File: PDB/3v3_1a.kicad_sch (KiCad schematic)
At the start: 13 parts, among them U17 INA228, U3 TLV62569ADRLR

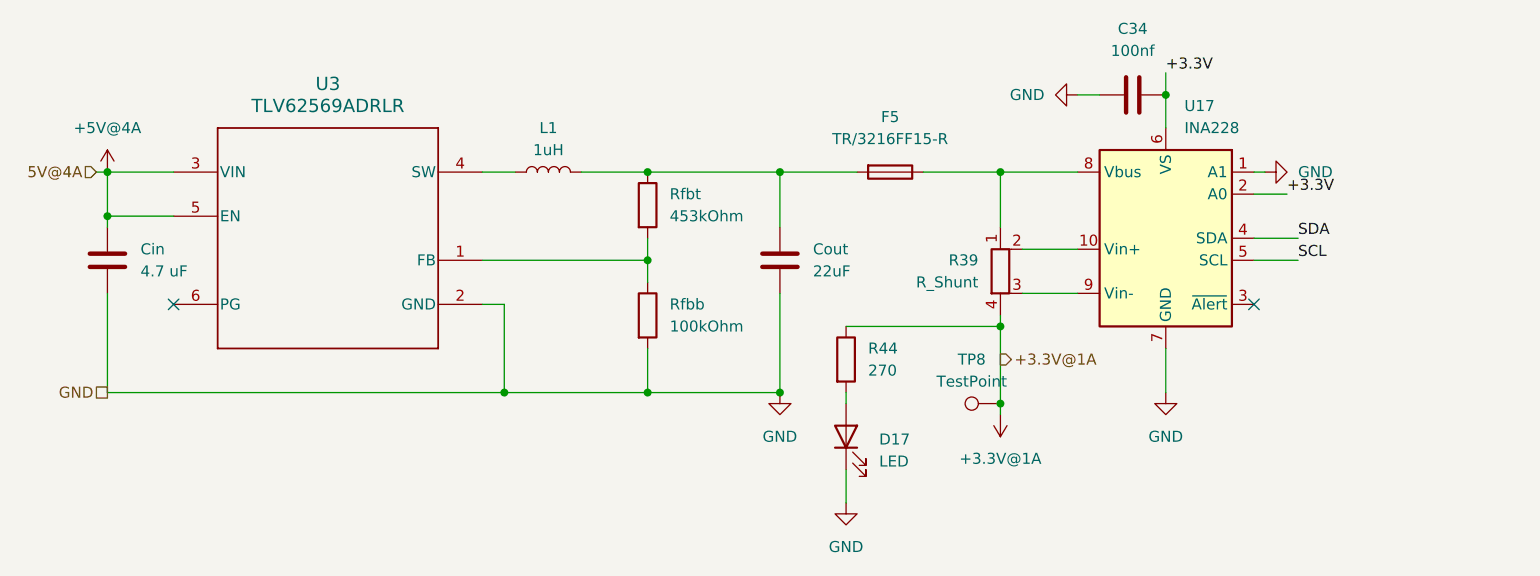
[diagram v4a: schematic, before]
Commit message: Finished all the footprints. doing poe myself now
finally.
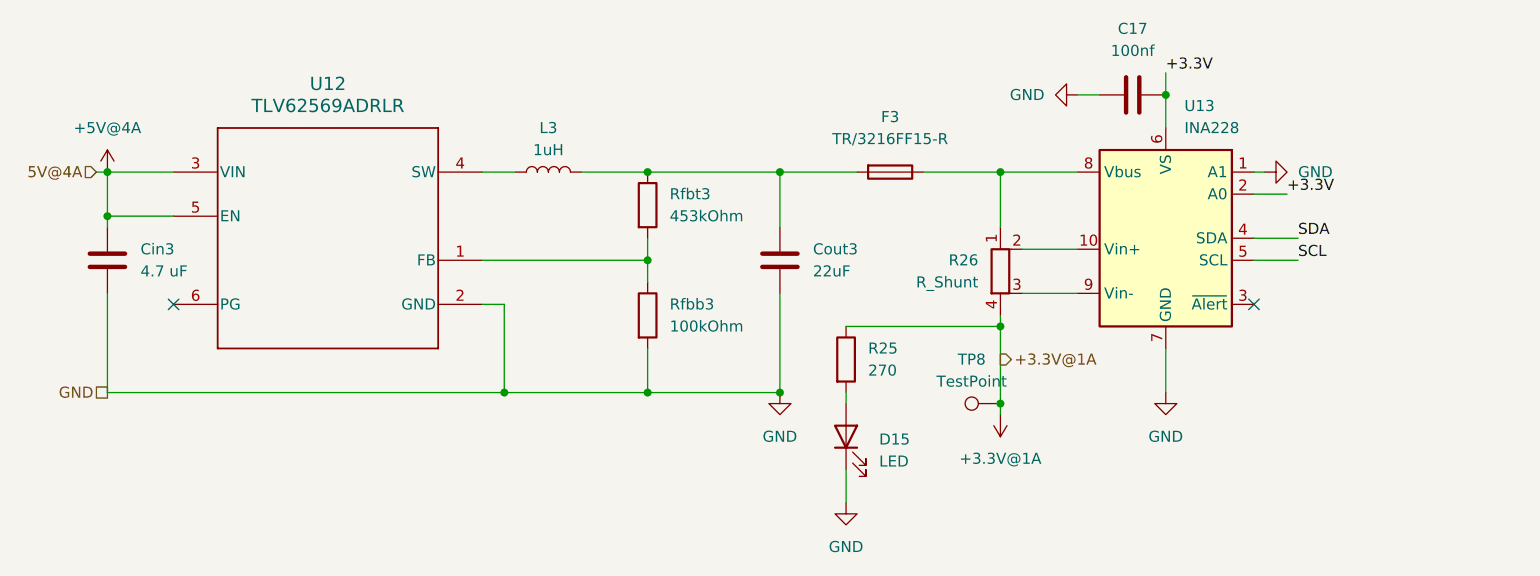
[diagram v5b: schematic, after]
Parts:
- C17: renamed from C34; footprint Capacitor_SMD:C_1206_3216Metric -> Capacitor_SMD:C_0603_1608Metric
- Cin3: renamed from Cin; footprint (none) -> Capacitor_SMD:C_0603_1608Metric
- Cout3: renamed from Cout; footprint (none) -> Capacitor_SMD:C_0603_1608Metric
- F3: renamed from F5; footprint (none) -> Fuse:Fuse_1206_3216Metric
- L3: renamed from L1; footprint (none) -> Inductor_SMD:L_1206_3216Metric
- R25: renamed from R44; footprint Resistor_SMD:R_1206_3216Metric_Pad1.30x1.75mm_HandSolder -> Resistor_SMD:R_0603_1608Metric
- R26: renamed from R39; footprint (none) -> Resistor_SMD:R_0603_1608Metric
- Rfbb3: renamed from Rfbb; footprint (none) -> Resistor_SMD:R_0603_1608Metric
- Rfbt3: renamed from Rfbt; footprint (none) -> Resistor_SMD:R_0603_1608Metric
- U12: renamed from U3; footprint DRL0006A -> Dependencies:TLV62569ADRLR
- U13: renamed from U17; footprint Package_SO:TSSOP-10_3x3mm_P0.5mm -> Package_SO:HVSSOP-10-1EP_3x3mm_P0.5mm_EP1.83x1.89mm
- renumbered D17 to D15
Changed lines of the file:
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@@
 		(dnp no)
 		(fields_autoplaced yes)
-		(property "Reference" "C34"
+		(property "Reference" "C17"
 			(at 151.13 43.18 90)
 			(show_name no)
@@
 			)
 		)
-		(property "Footprint" "Capacitor_SMD:C_1206_3216Metric"
+		(property "Footprint" "Capacitor_SMD:C_0603_1608Metric"
 			(at 154.94 49.8348 0)
 			(hide yes)
@@
 			(project "PDB"
 				(path "/a9cf05c4-aac5-4cf1-b700-1d3045f8dfbd/eaf0840f-875c-44d4-b065-16bc98c2c6be"
-					(reference "C34")
+					(reference "C17")
 					(unit 1)
 				)
@@
 		(dnp no)
 		(fields_autoplaced yes)
-		(property "Reference" "Cin"
+		(property "Reference" "Cin3"
 			(at 36.83 68.5799 0)
 			(show_name no)
@@
 			)
 		)
-		(property "Footprint" ""
+		(property "Footprint" "Capacitor_SMD:C_0603_1608Metric"
 			(at 33.9852 73.66 0)
 			(hide yes)
@@
 			(project "PDB"
 				(path "/a9cf05c4-aac5-4cf1-b700-1d3045f8dfbd/eaf0840f-875c-44d4-b065-16bc98c2c6be"
-					(reference "Cin")
+					(reference "Cin3")
 					(unit 1)
 				)
@@
 		(dnp no)
 		(fields_autoplaced yes)
-		(property "Reference" "U3"
+		(property "Reference" "U12"
 			(at 58.42 49.53 0)
 			(show_name no)
@@
 			)
 		)
-		(property "Footprint" "DRL0006A"
+		(property "Footprint" "Dependencies:TLV62569ADRLR"
 			(at 58.42 67.31 0)
 			(hide yes)
@@
 			(project "PDB"
 				(path "/a9cf05c4-aac5-4cf1-b700-1d3045f8dfbd/eaf0840f-875c-44d4-b065-16bc98c2c6be"
-					(reference "U3")
+					(reference "U12")
 					(unit 1)
 				)
@@
 		(dnp no)
 		(fields_autoplaced yes)
-		(property "Reference" "Rfbt"
+		(property "Reference" "Rfbt3"
 			(at 97.79 62.2299 0)
 			(show_name no)
@@
 			)
 		)
-		(property "Footprint" ""
+		(property "Footprint" "Resistor_SMD:R_0603_1608Metric"
 			(at 93.472 63.5 90)
 			(hide yes)
@@
 			(project "PDB"
 				(path "/a9cf05c4-aac5-4cf1-b700-1d3045f8dfbd/eaf0840f-875c-44d4-b065-16bc98c2c6be"
-					(reference "Rfbt")
+					(reference "Rfbt3")
 					(unit 1)
 				)
@@
 		(dnp no)
 		(fields_autoplaced yes)
-		(property "Reference" "R39"
+		(property "Reference" "R26"
 			(at 133.35 69.8499 0)
 			(show_name no)
@@
 			)
 		)
-		(property "Footprint" ""
+		(property "Footprint" "Resistor_SMD:R_0603_1608Metric"
 			(at 134.112 71.12 90)
 			(hide yes)
@@
 			(project "PDB"
 				(path "/a9cf05c4-aac5-4cf1-b700-1d3045f8dfbd/eaf0840f-875c-44d4-b065-16bc98c2c6be"
-					(reference "R39")
+					(reference "R26")
 					(unit 1)
 				)
@@
 		(dnp no)
 		(fields_autoplaced yes)
-		(property "Reference" "F5"
+		(property "Reference" "F3"
 			(at 123.19 53.34 90)
 			(show_name no)
@@
 			)
 		)
-		(property "Footprint" ""
+		(property "Footprint" "Fuse:Fuse_1206_3216Metric"
 			(at 123.19 57.912 90)
 			(hide yes)
@@
 			(project "PDB"
 				(path "/a9cf05c4-aac5-4cf1-b700-1d3045f8dfbd/eaf0840f-875c-44d4-b065-16bc98c2c6be"
-					(reference "F5")
+					(reference "F3")
 					(unit 1)
 				)
@@
 		(dnp no)
 		(fields_autoplaced yes)
-		(property "Reference" "Cout"
+		(property "Reference" "Cout3"
 			(at 114.3 68.5799 0)
 			(show_name no)
@@
 			)
 		)
-		(property "Footprint" ""
+		(property "Footprint" "Capacitor_SMD:C_0603_1608Metric"
 			(at 111.4552 73.66 0)
 			(hide yes)
@@
 			(project "PDB"
 				(path "/a9cf05c4-aac5-4cf1-b700-1d3045f8dfbd/eaf0840f-875c-44d4-b065-16bc98c2c6be"
-					(reference "Cout")
+					(reference "Cout3")
 					(unit 1)
 				)
@@
 		(in_pos_files yes)
 		(dnp no)
-		(property "Reference" "R44"
+		(property "Reference" "R25"
 			(at 120.65 80.0099 0)
 			(show_name no)
@@
 			)
 		)
-		(property "Footprint" "Resistor_SMD:R_1206_3216Metric_Pad1.30x1.75mm_HandSolder"
+		(property "Footprint" "Resistor_SMD:R_0603_1608Metric"
 			(at 116.332 81.28 90)
 			(hide yes)
@@
 			(project "PDB"
 				(path "/a9cf05c4-aac5-4cf1-b700-1d3045f8dfbd/eaf0840f-875c-44d4-b065-16bc98c2c6be"
-					(reference "R44")
+					(reference "R25")
 					(unit 1)
 				)
@@
 		(dnp no)
 		(fields_autoplaced yes)
-		(property "Reference" "Rfbb"
+		(property "Reference" "Rfbb3"
 			(at 97.79 74.9299 0)
 			(show_name no)
@@
 			)
 		)
-		(property "Footprint" ""
+		(property "Footprint" "Resistor_SMD:R_0603_1608Metric"
 			(at 93.472 76.2 90)
 			(hide yes)
@@
 			(project "PDB"
 				(path "/a9cf05c4-aac5-4cf1-b700-1d3045f8dfbd/eaf0840f-875c-44d4-b065-16bc98c2c6be"
-					(reference "Rfbb")
+					(reference "Rfbb3")
 					(unit 1)
 				)
@@
 		(dnp no)
 		(fields_autoplaced yes)
-		(property "Reference" "L1"
+		(property "Reference" "L3"
 			(at 83.82 54.61 90)
 			(show_name no)
@@
 			)
 		)
-		(property "Footprint" ""
+		(property "Footprint" "Inductor_SMD:L_1206_3216Metric"
 			(at 83.82 59.69 0)
 			(hide yes)
@@
 			(project "PDB"
 				(path "/a9cf05c4-aac5-4cf1-b700-1d3045f8dfbd/eaf0840f-875c-44d4-b065-16bc98c2c6be"
-					(reference "L1")
+					(reference "L3")
 					(unit 1)
 				)
@@
 		(dnp no)
 		(fields_autoplaced yes)
-		(property "Reference" "D17"
+		(property "Reference" "D15"
 			(at 121.92 90.4874 90)
 			(show_name no)
@@
 			(project "PDB"
 				(path "/a9cf05c4-aac5-4cf1-b700-1d3045f8dfbd/eaf0840f-875c-44d4-b065-16bc98c2c6be"
-					(reference "D17")
+					(reference "D15")
 					(unit 1)
 				)
@@
 		(dnp no)
 		(fields_autoplaced yes)
-		(property "Reference" "U17"
+		(property "Reference" "U13"
 			(at 157.0833 52.07 0)
 			(show_name no)
@@
 			)
 		)
-		(property "Footprint" "Package_SO:TSSOP-10_3x3mm_P0.5mm"
+		(property "Footprint" "Package_SO:HVSSOP-10-1EP_3x3mm_P0.5mm_EP1.83x1.89mm"
 			(at 179.832 44.704 0)
 			(hide yes)
@@
 			(project "PDB"
 				(path "/a9cf05c4-aac5-4cf1-b700-1d3045f8dfbd/eaf0840f-875c-44d4-b065-16bc98c2c6be"
-					(reference "U17")
-					(unit 1)
-				)
+					(reference "U13")
+					(unit 1)
+				)

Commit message: fixed component footprints
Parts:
- R26: footprint Resistor_SMD:R_0603_1608Metric -> Resistor_SMD:R_Shunt_Vishay_WSR2_WSR3_KelvinConnection
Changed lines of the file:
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@@
 		(dnp no)
 		(fields_autoplaced yes)
-		(property "Reference" "#PWR06"
+		(property "Reference" "#PWR058"
 			(at 110.49 91.44 0)
 			(hide yes)
@@
 			(project "PDB"
 				(path "/a9cf05c4-aac5-4cf1-b700-1d3045f8dfbd/eaf0840f-875c-44d4-b065-16bc98c2c6be"
-					(reference "#PWR06")
+					(reference "#PWR058")
 					(unit 1)
 				)
@@
 		(dnp no)
 		(fields_autoplaced yes)
-		(property "Reference" "#PWR059"
+		(property "Reference" "#PWR063"
 			(at 172.72 59.69 0)
 			(hide yes)
@@
 			(project "PDB"
 				(path "/a9cf05c4-aac5-4cf1-b700-1d3045f8dfbd/eaf0840f-875c-44d4-b065-16bc98c2c6be"
-					(reference "#PWR059")
+					(reference "#PWR063")
 					(unit 1)
 				)
@@
 		(dnp no)
 		(fields_autoplaced yes)
-		(property "Reference" "#PWR060"
+		(property "Reference" "#PWR062"
 			(at 154.94 91.44 0)
 			(hide yes)
@@
 			(project "PDB"
 				(path "/a9cf05c4-aac5-4cf1-b700-1d3045f8dfbd/eaf0840f-875c-44d4-b065-16bc98c2c6be"
-					(reference "#PWR060")
+					(reference "#PWR062")
 					(unit 1)
 				)
@@
 			)
 		)
-		(property "Footprint" "Resistor_SMD:R_0603_1608Metric"
+		(property "Footprint" "Resistor_SMD:R_Shunt_Vishay_WSR2_WSR3_KelvinConnection"
 			(at 134.112 71.12 90)
 			(hide yes)
@@
 		(dnp no)
 		(fields_autoplaced yes)
-		(property "Reference" "#PWR09"
+		(property "Reference" "#PWR060"
 			(at 135.89 83.82 0)
 			(hide yes)
@@
 			(project "PDB"
 				(path "/a9cf05c4-aac5-4cf1-b700-1d3045f8dfbd/eaf0840f-875c-44d4-b065-16bc98c2c6be"
-					(reference "#PWR09")
+					(reference "#PWR060")
 					(unit 1)
 				)
@@
 		(dnp no)
 		(fields_autoplaced yes)
-		(property "Reference" "#PWR058"
+		(property "Reference" "#PWR061"
 			(at 138.43 50.8 0)
 			(hide yes)
@@
 			(project "PDB"
 				(path "/a9cf05c4-aac5-4cf1-b700-1d3045f8dfbd/eaf0840f-875c-44d4-b065-16bc98c2c6be"
-					(reference "#PWR058")
+					(reference "#PWR061")
 					(unit 1)
 				)
@@
 		(dnp no)
 		(fields_autoplaced yes)
-		(property "Reference" "#PWR05"
+		(property "Reference" "#PWR057"
 			(at 33.02 63.5 0)
 			(hide yes)
@@
 			(project "PDB"
 				(path "/a9cf05c4-aac5-4cf1-b700-1d3045f8dfbd/eaf0840f-875c-44d4-b065-16bc98c2c6be"
-					(reference "#PWR05")
+					(reference "#PWR057")
 					(unit 1)
 				)
@@
 		(dnp no)
 		(fields_autoplaced yes)
-		(property "Reference" "#PWR071"
+		(property "Reference" "#PWR059"
 			(at 118.11 104.14 0)
 			(hide yes)
@@
 			(project "PDB"
 				(path "/a9cf05c4-aac5-4cf1-b700-1d3045f8dfbd/eaf0840f-875c-44d4-b065-16bc98c2c6be"
-					(reference "#PWR071")
-					(unit 1)
-				)
+					(reference "#PWR059")
+					(unit 1)
+				)

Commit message: laid out many, many things
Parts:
- R26: footprint Resistor_SMD:R_Shunt_Vishay_WSR2_WSR3_KelvinConnection -> Resistor_SMD:R_Shunt_Vishay_WSK2512_6332Metric_T2.66mm
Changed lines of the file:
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@@
 			)
 		)
-		(property "Footprint" "Resistor_SMD:R_Shunt_Vishay_WSR2_WSR3_KelvinConnection"
+		(property "Footprint" "Resistor_SMD:R_Shunt_Vishay_WSK2512_6332Metric_T2.66mm"
 			(at 134.112 71.12 90)
 			(hide yes)

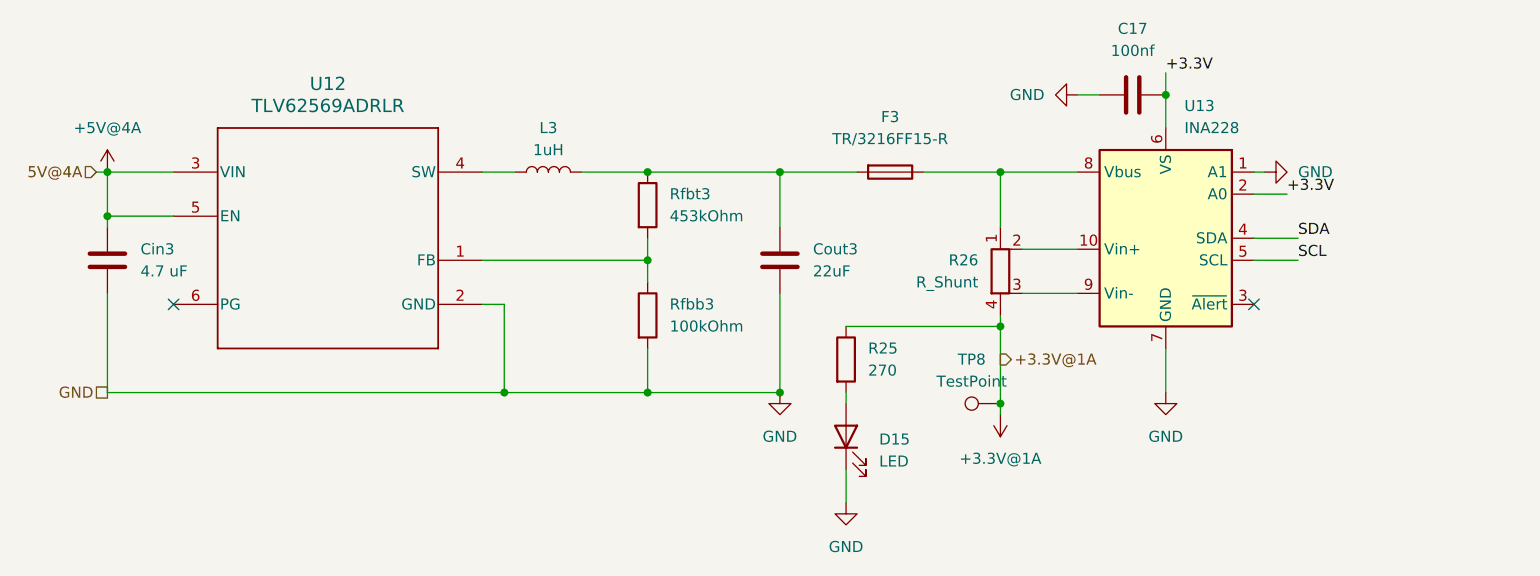
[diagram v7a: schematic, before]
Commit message: coordinated labels in schem
Labeled all components to be Rxx, Cxx, ext forms through all sheets so labels for BOM and layout are work together as one long list.
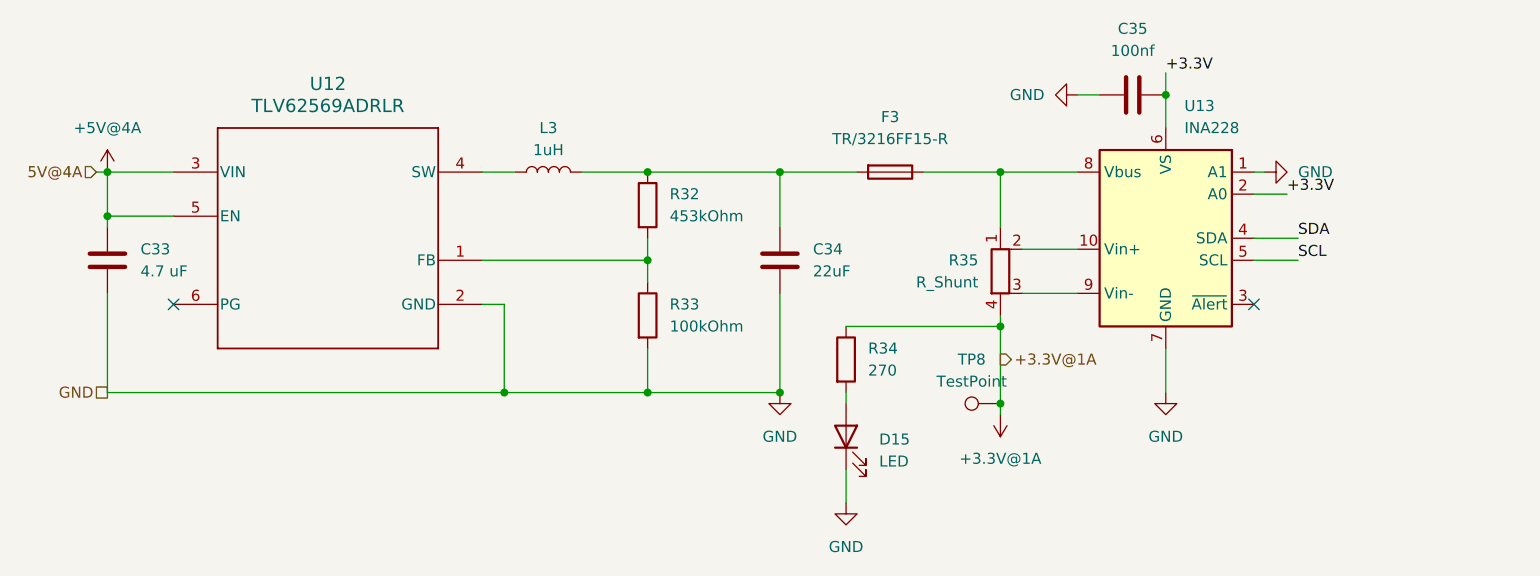
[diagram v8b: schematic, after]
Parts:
- renumbered Cin3 to C33, Cout3 to C34, C17 to C35, Rfbt3 to R32, Rfbb3 to R33, R25 to R34, R26 to R35
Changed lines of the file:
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@@
 		(dnp no)
 		(fields_autoplaced yes)
-		(property "Reference" "#PWR058"
+		(property "Reference" "#PWR059"
 			(at 110.49 91.44 0)
 			(hide yes)
@@
 			(project "PDB"
 				(path "/a9cf05c4-aac5-4cf1-b700-1d3045f8dfbd/eaf0840f-875c-44d4-b065-16bc98c2c6be"
-					(reference "#PWR058")
+					(reference "#PWR059")
 					(unit 1)
 				)
@@
 		(dnp no)
 		(fields_autoplaced yes)
-		(property "Reference" "C17"
+		(property "Reference" "C35"
 			(at 151.13 43.18 90)
 			(show_name no)
@@
 			(project "PDB"
 				(path "/a9cf05c4-aac5-4cf1-b700-1d3045f8dfbd/eaf0840f-875c-44d4-b065-16bc98c2c6be"
-					(reference "C17")
+					(reference "C35")
 					(unit 1)
 				)
@@
 		(dnp no)
 		(fields_autoplaced yes)
-		(property "Reference" "#PWR063"
+		(property "Reference" "#PWR064"
 			(at 172.72 59.69 0)
 			(hide yes)
@@
 			(project "PDB"
 				(path "/a9cf05c4-aac5-4cf1-b700-1d3045f8dfbd/eaf0840f-875c-44d4-b065-16bc98c2c6be"
-					(reference "#PWR063")
+					(reference "#PWR064")
 					(unit 1)
 				)
@@
 		(dnp no)
 		(fields_autoplaced yes)
-		(property "Reference" "Cin3"
+		(property "Reference" "C33"
 			(at 36.83 68.5799 0)
 			(show_name no)
@@
 			(project "PDB"
 				(path "/a9cf05c4-aac5-4cf1-b700-1d3045f8dfbd/eaf0840f-875c-44d4-b065-16bc98c2c6be"
-					(reference "Cin3")
+					(reference "C33")
 					(unit 1)
 				)
@@
 		(dnp no)
 		(fields_autoplaced yes)
-		(property "Reference" "#PWR062"
+		(property "Reference" "#PWR063"
 			(at 154.94 91.44 0)
 			(hide yes)
@@
 			(project "PDB"
 				(path "/a9cf05c4-aac5-4cf1-b700-1d3045f8dfbd/eaf0840f-875c-44d4-b065-16bc98c2c6be"
-					(reference "#PWR062")
+					(reference "#PWR063")
 					(unit 1)
 				)
@@
 		(dnp no)
 		(fields_autoplaced yes)
-		(property "Reference" "Rfbt3"
+		(property "Reference" "R32"
 			(at 97.79 62.2299 0)
 			(show_name no)
@@
 			(project "PDB"
 				(path "/a9cf05c4-aac5-4cf1-b700-1d3045f8dfbd/eaf0840f-875c-44d4-b065-16bc98c2c6be"
-					(reference "Rfbt3")
+					(reference "R32")
 					(unit 1)
 				)
@@
 		(dnp no)
 		(fields_autoplaced yes)
-		(property "Reference" "R26"
+		(property "Reference" "R35"
 			(at 133.35 69.8499 0)
 			(show_name no)
@@
 			(project "PDB"
 				(path "/a9cf05c4-aac5-4cf1-b700-1d3045f8dfbd/eaf0840f-875c-44d4-b065-16bc98c2c6be"
-					(reference "R26")
+					(reference "R35")
 					(unit 1)
 				)
@@
 		(dnp no)
 		(fields_autoplaced yes)
-		(property "Reference" "#PWR060"
+		(property "Reference" "#PWR061"
 			(at 135.89 83.82 0)
 			(hide yes)
@@
 			(project "PDB"
 				(path "/a9cf05c4-aac5-4cf1-b700-1d3045f8dfbd/eaf0840f-875c-44d4-b065-16bc98c2c6be"
-					(reference "#PWR060")
+					(reference "#PWR061")
 					(unit 1)
 				)
@@
 		(dnp no)
 		(fields_autoplaced yes)
-		(property "Reference" "#PWR061"
+		(property "Reference" "#PWR062"
 			(at 138.43 50.8 0)
 			(hide yes)
@@
 			(project "PDB"
 				(path "/a9cf05c4-aac5-4cf1-b700-1d3045f8dfbd/eaf0840f-875c-44d4-b065-16bc98c2c6be"
-					(reference "#PWR061")
+					(reference "#PWR062")
 					(unit 1)
 				)
@@
 		(dnp no)
 		(fields_autoplaced yes)
-		(property "Reference" "#PWR057"
+		(property "Reference" "#PWR058"
 			(at 33.02 63.5 0)
 			(hide yes)
@@
 			(project "PDB"
 				(path "/a9cf05c4-aac5-4cf1-b700-1d3045f8dfbd/eaf0840f-875c-44d4-b065-16bc98c2c6be"
-					(reference "#PWR057")
+					(reference "#PWR058")
 					(unit 1)
 				)
@@
 		(dnp no)
 		(fields_autoplaced yes)
-		(property "Reference" "Cout3"
+		(property "Reference" "C34"
 			(at 114.3 68.5799 0)
 			(show_name no)
@@
 			(project "PDB"
 				(path "/a9cf05c4-aac5-4cf1-b700-1d3045f8dfbd/eaf0840f-875c-44d4-b065-16bc98c2c6be"
-					(reference "Cout3")
+					(reference "C34")
 					(unit 1)
 				)
@@
 		(dnp no)
 		(fields_autoplaced yes)
-		(property "Reference" "#PWR059"
+		(property "Reference" "#PWR060"
 			(at 118.11 104.14 0)
 			(hide yes)
@@
 			(project "PDB"
 				(path "/a9cf05c4-aac5-4cf1-b700-1d3045f8dfbd/eaf0840f-875c-44d4-b065-16bc98c2c6be"
-					(reference "#PWR059")
+					(reference "#PWR060")
 					(unit 1)
 				)
@@
 		(in_pos_files yes)
 		(dnp no)
-		(property "Reference" "R25"
+		(property "Reference" "R34"
 			(at 120.65 80.0099 0)
 			(show_name no)
@@
 			(project "PDB"
 				(path "/a9cf05c4-aac5-4cf1-b700-1d3045f8dfbd/eaf0840f-875c-44d4-b065-16bc98c2c6be"
-					(reference "R25")
+					(reference "R34")
 					(unit 1)
 				)
@@
 		(dnp no)
 		(fields_autoplaced yes)
-		(property "Reference" "Rfbb3"
+		(property "Reference" "R33"
 			(at 97.79 74.9299 0)
 			(show_name no)
@@
 			(project "PDB"
 				(path "/a9cf05c4-aac5-4cf1-b700-1d3045f8dfbd/eaf0840f-875c-44d4-b065-16bc98c2c6be"
-					(reference "Rfbb3")
-					(unit 1)
-				)
+					(reference "R33")
+					(unit 1)
+				)
